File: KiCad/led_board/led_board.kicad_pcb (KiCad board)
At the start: 2 copper layers, 99.8 x 100.8 mm, 121 parts, among them U1 74HC245, U2 74HC245, U3 74HC245, U4 74HC245, U5 74HC245, U6 74HC245, U7 74HC245, X1 Edge72

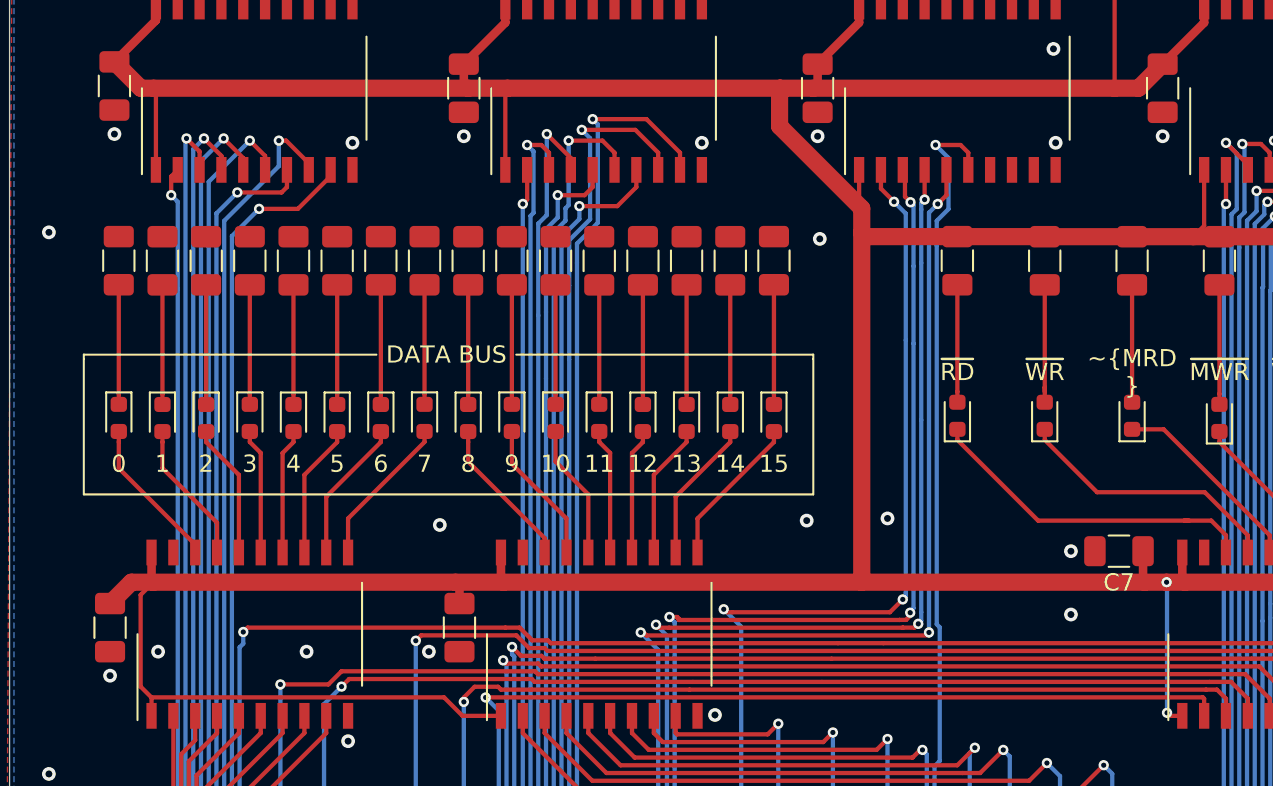
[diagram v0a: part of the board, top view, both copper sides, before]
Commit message: Minor changes at I/O board, LED board and VGA
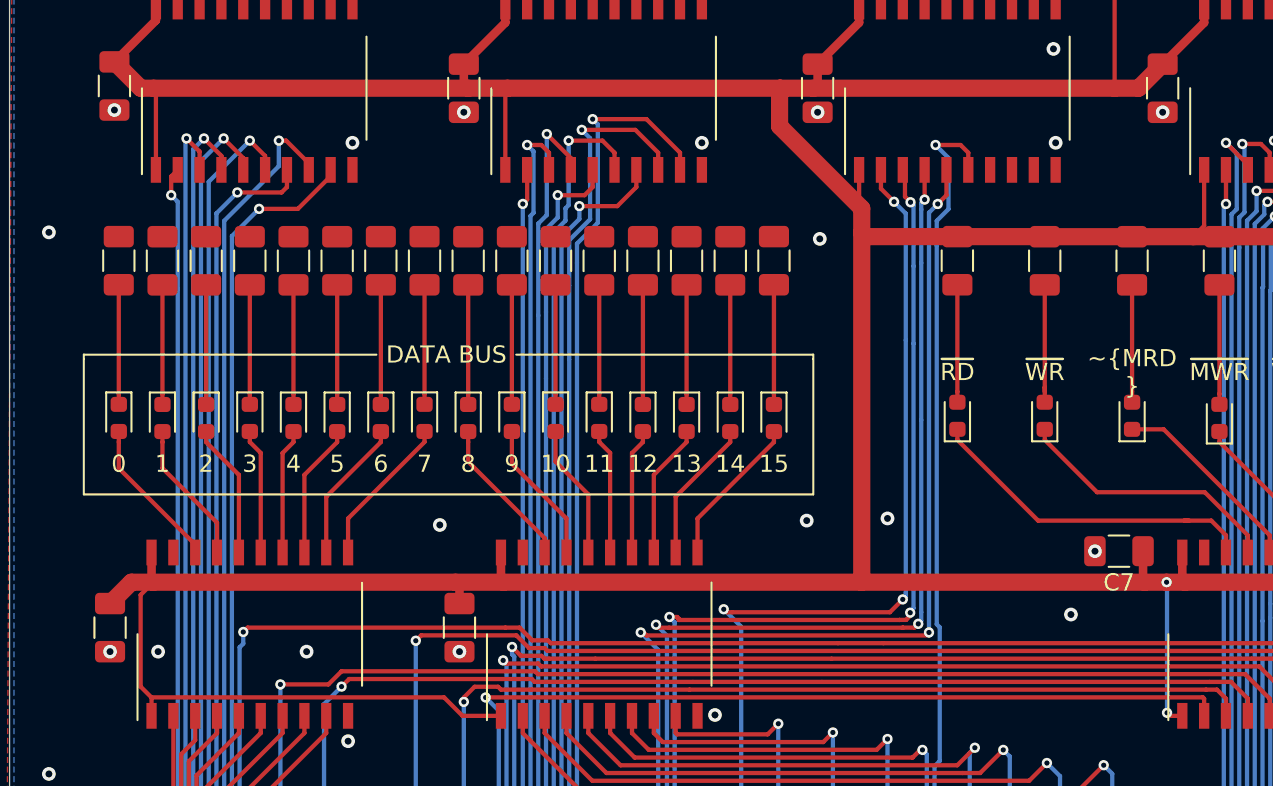
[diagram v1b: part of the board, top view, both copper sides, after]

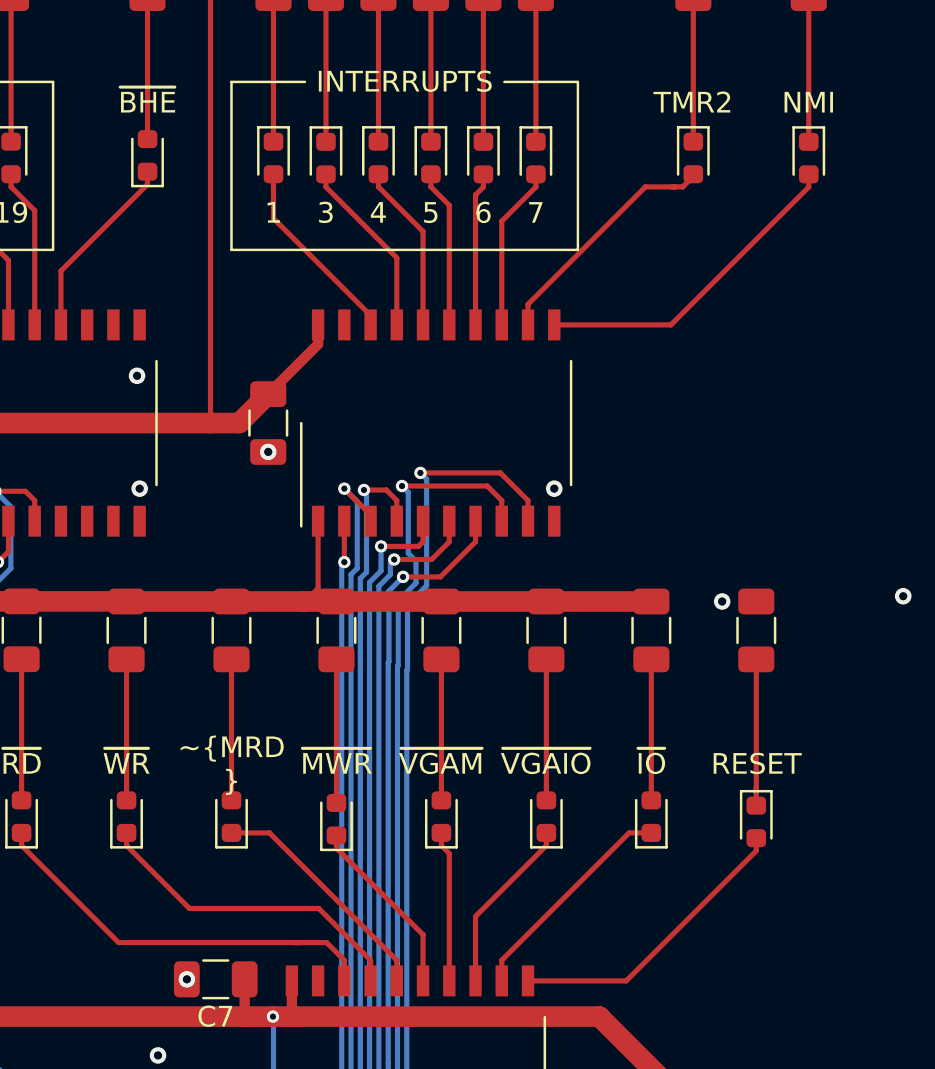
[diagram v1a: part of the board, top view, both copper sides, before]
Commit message: Migration from KiCad 5 to KiCad 7
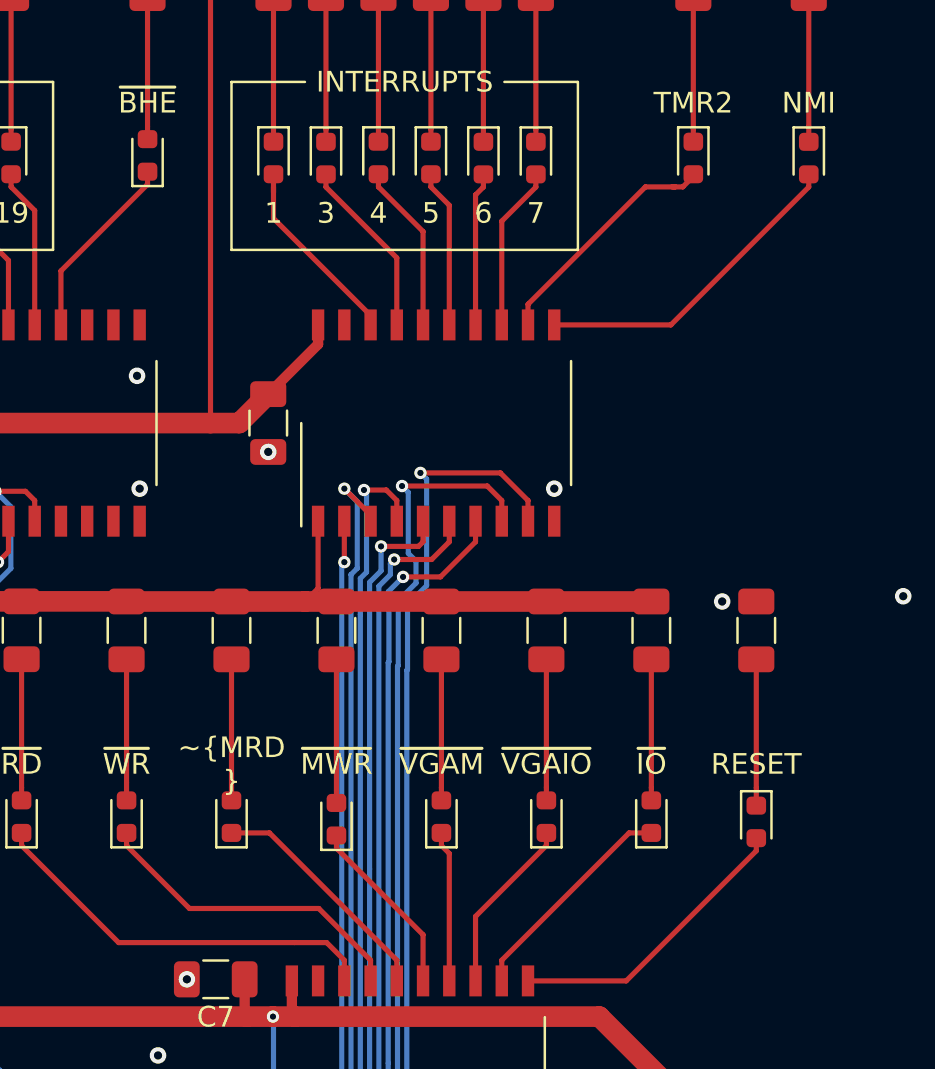
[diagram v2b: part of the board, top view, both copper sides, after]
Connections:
- net M_~IO renamed M_~{IO}
- net ~BHE renamed ~{BHE}
- net ~MEMRD renamed ~{MEMRD}
- net ~MEMWR renamed ~{MEMWR}
- net ~RD renamed ~{RD}
- net ~VGA_IO renamed ~{VGA_IO}
- net ~VGA_MEM renamed ~{VGA_MEM}
- net ~WR renamed ~{WR}
- U3 pad 11: Net-(U3-Pad11) -> unconnected-(U3-B7-Pad11)
- U3 pad 12: Net-(U3-Pad12) -> unconnected-(U3-B6-Pad12)
- U3 pad 13: Net-(U3-Pad13) -> unconnected-(U3-B5-Pad13)
- X1 pad 25: Net-(X1-Pad25) -> unconnected-(X1-N/C-Pad25)
- X1 pad 28: Net-(X1-Pad28) -> unconnected-(X1-RDY1-Pad28)
- X1 pad 29: Net-(X1-Pad29) -> unconnected-(X1-RDY2-Pad29)
- X1 pad 30: Net-(X1-Pad30) -> unconnected-(X1-PCLK-Pad30)
- X1 pad 31: Net-(X1-Pad31) -> unconnected-(X1-~{IO_DBG}-Pad31)
- X1 pad 34: Net-(X1-Pad34) -> unconnected-(X1-N/C-Pad34)
- X1 pad 70: Net-(X1-Pad70) -> unconnected-(X1-N/C-Pad70)
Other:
- net class Default removed
- board text added: "~{BHE}"
- board text added: "~{IO}"
- board text added: "~{MRD }"
- board text added: "~{MWR}"
- board text added: "~{RD}"
- board text added: "~{VGAIO}"
- board text added: "~{VGAM}"
- board text added: "~{WR}"
- board text removed: "~BHE"
- board text removed: "~IO"
- board text removed: "~MRD"
- board text removed: "~MWR"
- board text removed: "~RD"
- board text removed: "~VGAIO"
- board text removed: "~VGAM"
- board text removed: "~WR"
